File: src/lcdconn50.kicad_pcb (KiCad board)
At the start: 2 copper layers, 51.3 x 14.7 mm, 8 parts, among them U1 CAT4002

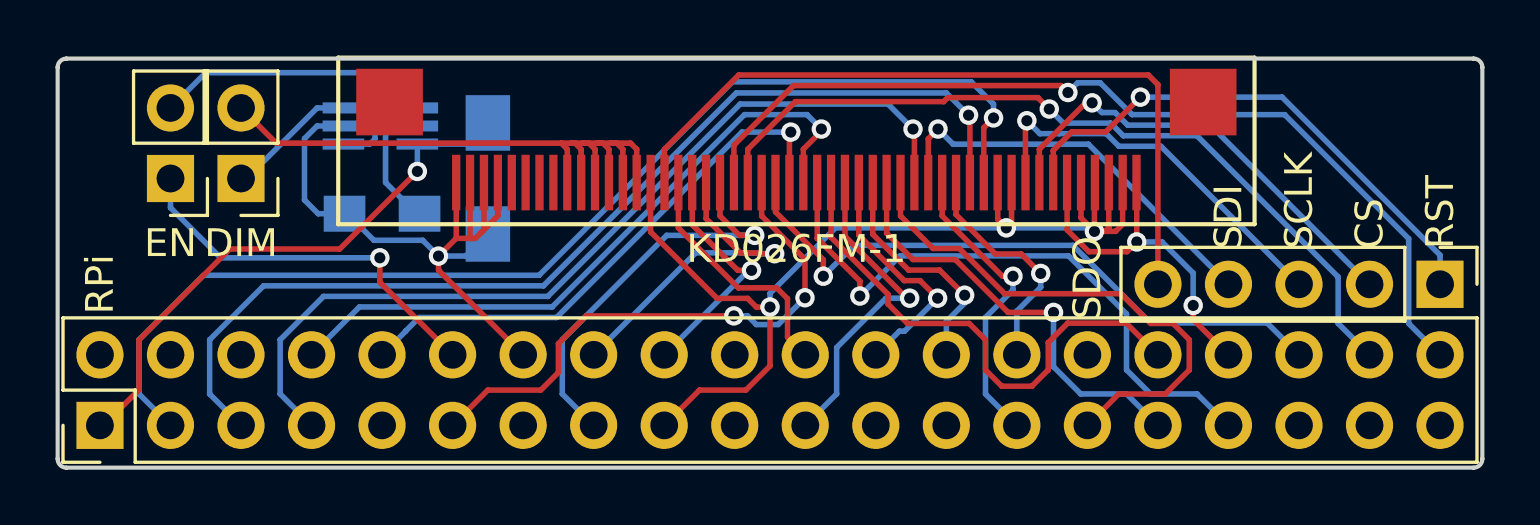
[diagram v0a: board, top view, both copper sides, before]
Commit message: New Release
Minor change to BCM_12 net.
Updated Image.

Signed-off-by: Mahyar Koshkouei <deltabeard@users.noreply.github.com>
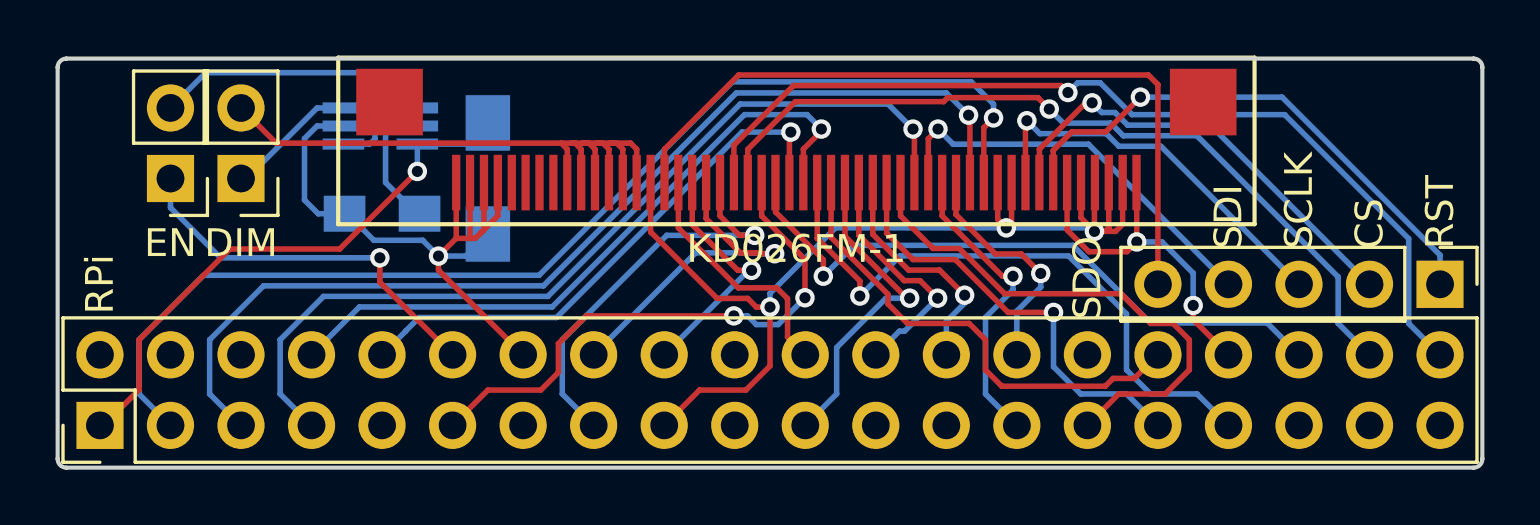
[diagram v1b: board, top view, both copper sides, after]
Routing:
- net /BCM_12: track 18.8 -> 17.3 mm
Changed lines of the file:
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@@
     (thickness 1.6)
     (drawings 16)
-    (tracks 380)
+    (tracks 378)
     (zones 0)
     (modules 8)
@@
     (title "Raspberry Pi LCD Connector for KD026-FM-1")
     (date 2017-06-24)
+    (rev 0.1)
     (company "Mahyar Koshkouei")
     (comment 1 "CC-BY-SA-4.0 License")
@@
   (segment (start 173.150001 68.7275) (end 173.150001 70.737081) (width 0.2) (layer F.Cu) (net 11) (status 10))
   (via (at 174.685807 72.814193) (size 0.7) (drill 0.4) (layers F.Cu B.Cu) (net 11))
+  (segment (start 173.650001 68.7275) (end 173.650001 70.699665) (width 0.2) (layer F.Cu) (net 12) (status 10))
+  (segment (start 173.650001 70.699665) (end 175.7 72.749664) (width 0.2) (layer F.Cu) (net 12))
+  (segment (start 175.7 72.749664) (end 175.7 73.1) (width 0.2) (layer F.Cu) (net 12))
+  (segment (start 184.570001 75.779999) (end 185.42 74.93) (width 0.2) (layer F.Cu) (net 12) (status 20))
   (segment (start 175.7 73.1) (end 176.399999 73.799999) (width 0.2) (layer F.Cu) (net 12))
-  (segment (start 175.7 72.749664) (end 175.7 73.1) (width 0.2) (layer F.Cu) (net 12))
+  (segment (start 176.399999 73.799999) (end 178.622399 73.799999) (width 0.2) (layer F.Cu) (net 12))
+  (segment (start 178.622399 73.799999) (end 179.209999 74.387599) (width 0.2) (layer F.Cu) (net 12))
+  (segment (start 179.797599 76.060001) (end 183.527999 76.060001) (width 0.2) (layer F.Cu) (net 12))
+  (segment (start 179.209999 74.387599) (end 179.209999 75.472401) (width 0.2) (layer F.Cu) (net 12))
   (segment (start 179.209999 75.472401) (end 179.797599 76.060001) (width 0.2) (layer F.Cu) (net 12))
-  (segment (start 184.280023 73.790023) (end 185.42 74.93) (width 0.2) (layer F.Cu) (net 12) (status 20))
-  (segment (start 181.470001 74.490364) (end 182.170342 73.790023) (width 0.2) (layer F.Cu) (net 12))
-  (segment (start 179.797599 76.060001) (end 180.882401 76.060001) (width 0.2) (layer F.Cu) (net 12))
-  (segment (start 179.209999 74.387599) (end 179.209999 75.472401) (width 0.2) (layer F.Cu) (net 12))
-  (segment (start 178.622399 73.799999) (end 179.209999 74.387599) (width 0.2) (layer F.Cu) (net 12))
-  (segment (start 173.650001 70.699665) (end 175.7 72.749664) (width 0.2) (layer F.Cu) (net 12))
-  (segment (start 181.470001 75.472401) (end 181.470001 74.490364) (width 0.2) (layer F.Cu) (net 12))
-  (segment (start 176.399999 73.799999) (end 178.622399 73.799999) (width 0.2) (layer F.Cu) (net 12))
-  (segment (start 173.650001 68.7275) (end 173.650001 70.699665) (width 0.2) (layer F.Cu) (net 12) (status 10))
-  (segment (start 182.170342 73.790023) (end 184.280023 73.790023) (width 0.2) (layer F.Cu) (net 12))
-  (segment (start 180.882401 76.060001) (end 181.470001 75.472401) (width 0.2) (layer F.Cu) (net 12))
+  (segment (start 183.527999 76.060001) (end 183.808001 75.779999) (width 0.2) (layer F.Cu) (net 12))
+  (segment (start 183.808001 75.779999) (end 184.570001 75.779999) (width 0.2) (layer F.Cu) (net 12))
   (segment (start 175.650001 70.550001) (end 176.6 71.5) (width 0.2) (layer F.Cu) (net 13))
   (segment (start 180.028612 73.403444) (end 181.660012 73.403444) (width 0.2) (layer F.Cu) (net 13))
